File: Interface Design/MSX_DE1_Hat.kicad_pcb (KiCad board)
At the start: 2 copper layers, 103 x 66 mm, 27 parts, among them J1 J1, J2 J2, J3 J3, J4 J4, J5 J5, J6 J6, U1 74LVC245A, U2 74LVC245A, U3 74LVC245A, U4 74LVC245A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

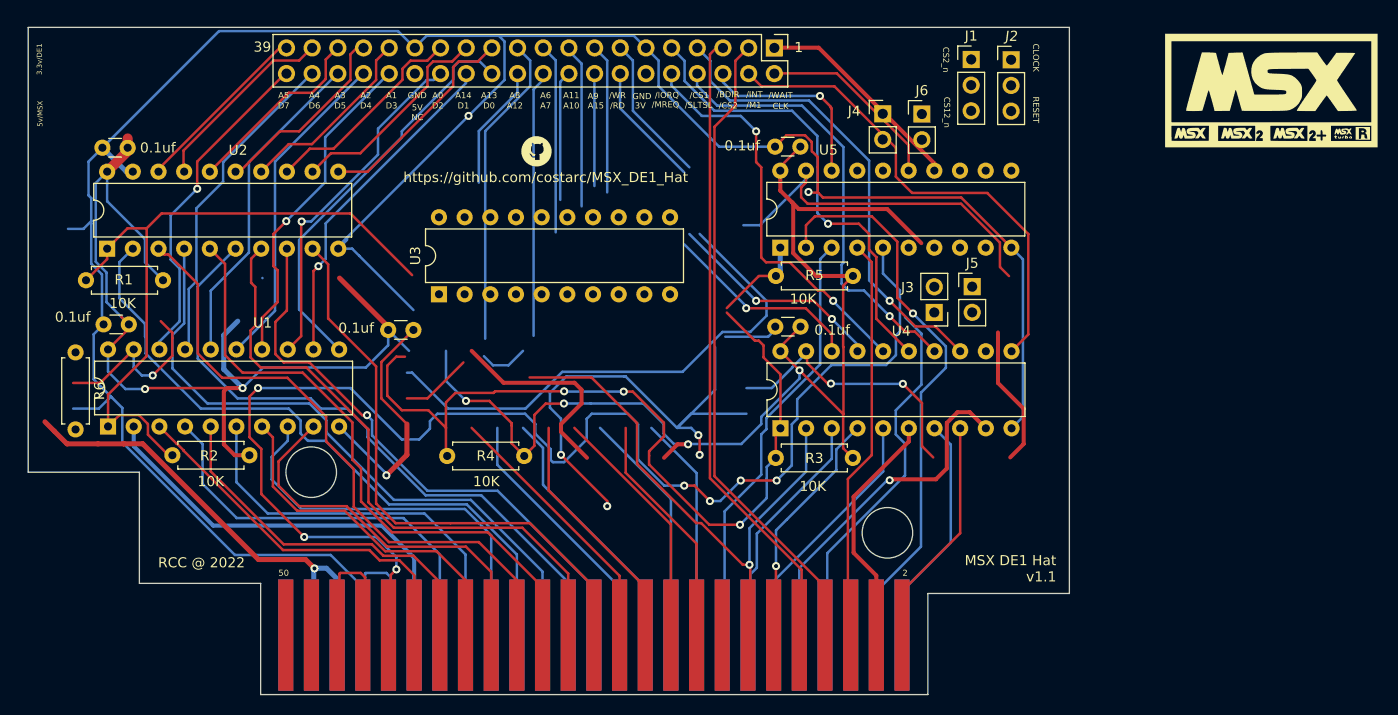
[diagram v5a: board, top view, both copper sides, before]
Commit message: Routing new pcb for v1.1
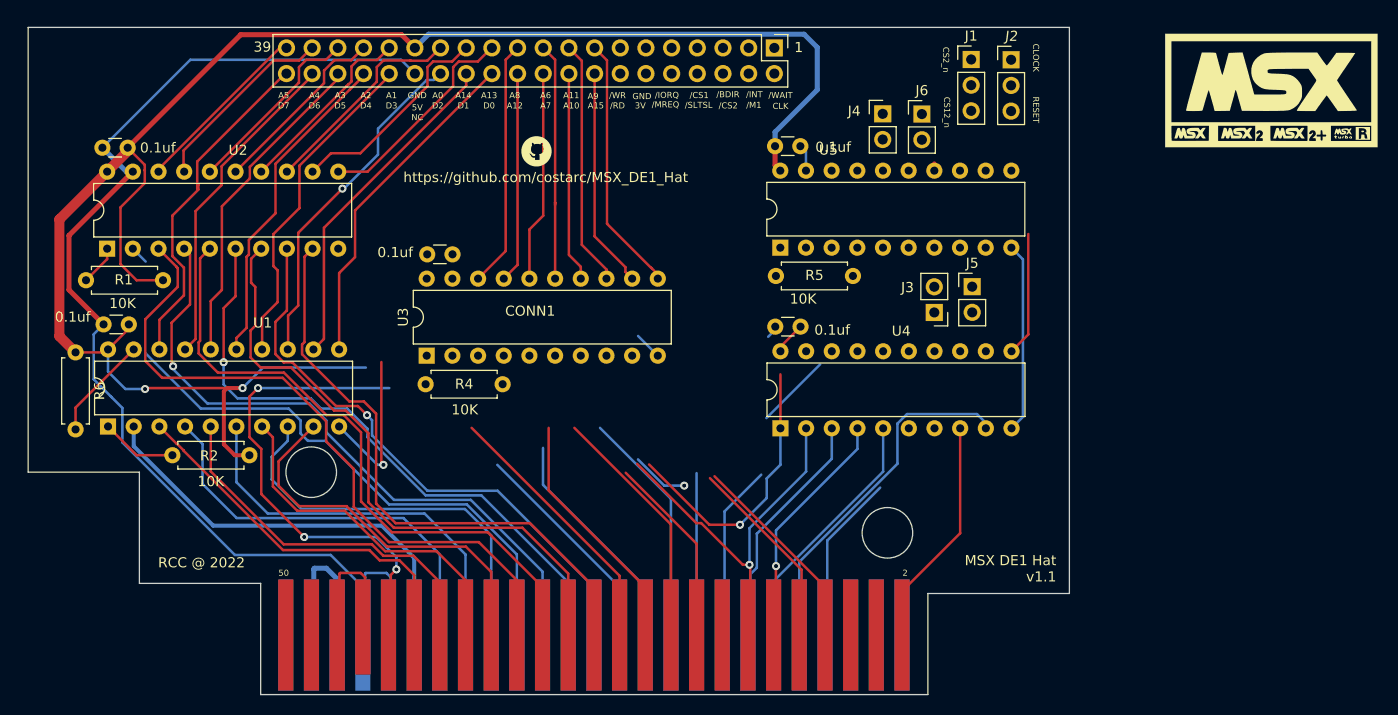
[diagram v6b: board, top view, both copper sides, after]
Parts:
- removed R3: 10K, Resistor_THT:R_Axial_DIN0207_L6.3mm_D2.5mm_P7.62mm_Horizontal
- CONN1: footprint Roni Footprints:MSX_CART -> Roni Footprints:MSX_CART_SW
- moved C3 8.42 mm to (93.9, 42.6)
- moved R4 7.41 mm to (98.9, 55.5)
- moved U3 6.19 mm to (91.4, 52.7)
- moved C5 2.50 mm to (128.3, 31.9), turned to 180 degrees
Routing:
- net GNDREF: track 405.7 -> 163.4 mm, vias 9 -> 1
- net CLOCK: track 134.8 -> 53.8 mm, vias 7 -> 4
- net Net-(R1-Pad2): track 68.4 -> 3.99 mm
- net /CS12: track 56.5 -> 0.00 mm, vias 1 -> 0
- net Net-(R3-Pad2): track 82.1 -> 28.0 mm, vias 3 -> 1
- net (no net): track 51.7 -> 0.00 mm
- net /C_CS1: track 46.6 -> 0.00 mm, vias 1 -> 0
- net /C_IORQ: track 46.0 -> 0.00 mm, vias 1 -> 0
- net /INT: track 64.3 -> 20.5 mm
- net /C_SLTSL: track 43.7 -> 0.03 mm, vias 1 -> 0
- net /BUSDIR: track 62.9 -> 19.5 mm
- net Net-(J5-Pad2): track 42.1 -> 0.00 mm
- net Net-(J3-Pad2): track 40.3 -> 0.00 mm
- net /C_MREQ: track 40.1 -> 0.00 mm, vias 2 -> 0
- net Vdd: track 219.9 -> 179.8 mm, vias 6 -> 2
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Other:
- board text removed: "3.3v/DE1"
- board text removed: "5v/MSX"

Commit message: Fabricatin files added for the PCB v1.1
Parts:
- removed CD4077 / XNOR Truth Table: LOGO, LOGO
- added R3: 10K, Resistor_THT:R_Axial_DIN0207_L6.3mm_D2.5mm_P7.62mm_Horizontal, F.Cu at (134.1, 62.6)
- IDC1: footprint Connector_PinHeader_2.54mm:PinHeader_2x20_P2.54mm_Vertical -> Connector_IDC:IDC-Header_2x20_P2.54mm_Vertical
- moved G*** 79.6 mm to (105.2, 64.9)
- moved C5 6.74 mm to (123.5, 36.7), turned to -90 degrees
- moved G*** 3.47 mm to (103.9, 35.5)
- moved J5 2.59 mm to (145.5, 48.4), turned to 180 degrees
- moved J4 2.58 mm to (136.5, 31.3), turned to 180 degrees
- moved J6 2.55 mm to (140.3, 31.3), turned to 180 degrees
- moved IDC1 2.00 mm to (125.7, 24.2)
- moved R1 1.60 mm to (66.9, 45.0)
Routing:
- net GNDREF: track 163.4 -> 329.9 mm, vias 1 -> 4
- net /C_BUSDIR: track 11.2 -> 123.0 mm
- net CLOCK: track 53.8 -> 110.9 mm, vias 4 -> 3
- net /RD: track 45.8 -> 102.9 mm
- net /CS12: track 0.00 -> 46.2 mm
- net /INT: track 20.5 -> 66.6 mm
- net /BUSDIR: track 19.5 -> 65.3 mm
- net /C_CS1: track 0.00 -> 44.2 mm
- net /C_SLTSL: track 0.03 -> 43.3 mm
- net /WAIT: track 17.0 -> 60.1 mm, vias 0 -> 3
- net /C_WR: track 0.00 -> 43.0 mm
- net /C_IORQ: track 0.00 -> 42.6 mm
- net Vdd: track 179.8 -> 220.9 mm, vias 2 -> 3
- net /C_CS2: track 0.00 -> 40.1 mm, vias 0 -> 1
- net /C_RD: track 0.00 -> 39.4 mm
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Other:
- board text added: "/IOQ"
- board text added: "/MRQ"
- board text added: "/SLT"
- board text added: "3.3v"
- board text added: "40"
- board text added: "NC/5V"
- board text added: "RCC @ 2023"
- board text removed: "/IORQ"
- board text removed: "/MREQ"
- board text removed: "/SLTSL"
- board text removed: "3V"
- board text removed: "5V NC"
- board text removed: "RCC @ 2022"

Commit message: Added Gerber files
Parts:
- CONN1: footprint Roni Footprints:MSX_CART_SW -> Roni Footprints:MSX_CART
- IDC1: footprint Connector_IDC:IDC-Header_2x20_P2.54mm_Vertical -> Connector_PinHeader_2.54mm:PinHeader_2x20_P2.54mm_Vertical
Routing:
- net GNDREF: track 329.9 -> 335.4 mm, vias 4 -> 6
- net CLOCK: track 110.9 -> 110.0 mm
- added copper zone on B.Cu, net GNDREF
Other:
- board text added: "MSX FPGA Hat DE1 v1.1"
- board text added: "https://github.com/costarc/MSX_FPGA_Hat"
- board text removed: "MSX DE1 Hat v1.1"
- board text removed: "https://github.com/costarc/MSX_DE1_Hat"
